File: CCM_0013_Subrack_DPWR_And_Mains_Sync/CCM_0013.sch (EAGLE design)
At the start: 12 parts, among them X15 MAB64

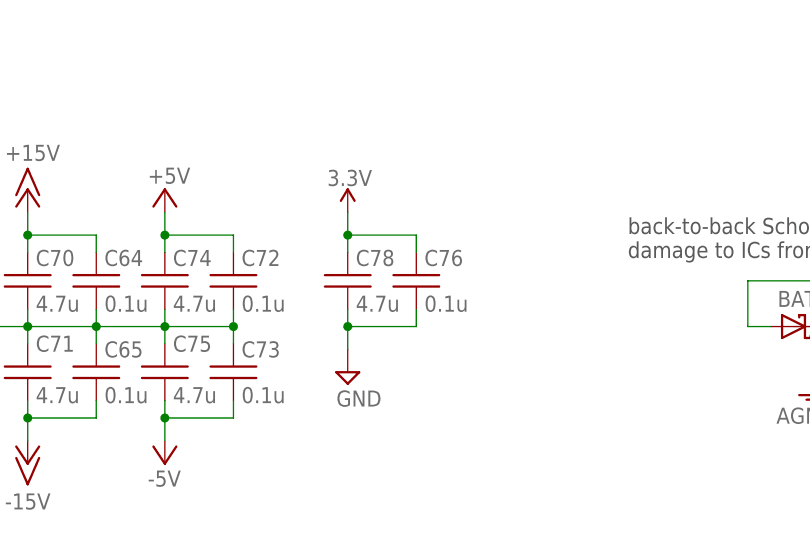
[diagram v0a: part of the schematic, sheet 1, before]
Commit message: Shutter driver added.
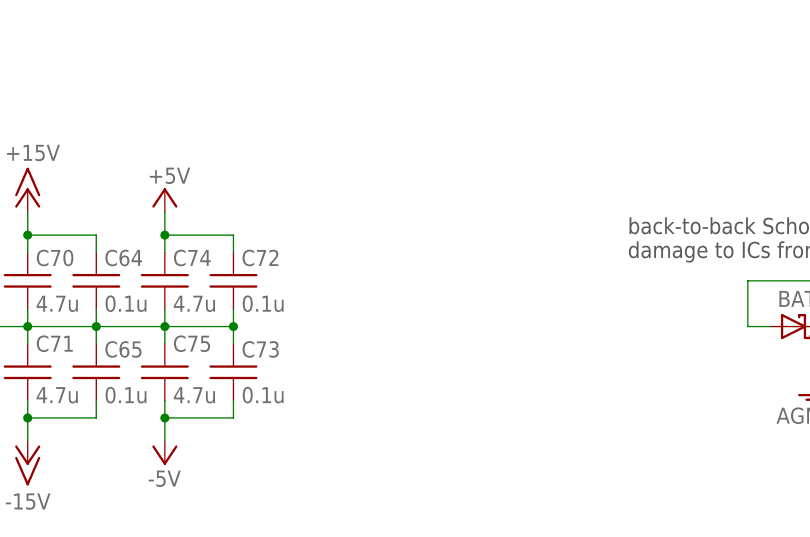
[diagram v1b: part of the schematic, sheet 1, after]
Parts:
- removed C76: 0.1u, acrooptics:C0603
- removed C78: 4.7u, acrooptics:C0603
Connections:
- removed net 3.3V: C76.1, C78.1
- net GND: no longer C76.2, C78.2
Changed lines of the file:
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@@
 <?xml version="1.0" encoding="utf-8"?>
 <!DOCTYPE eagle SYSTEM "eagle.dtd">
-<eagle version="8.6.0">
+<eagle version="9.0.1">
 <drawing>
 <settings>
@@
 <setting verticaltext="up"/>
 </settings>
-<grid distance="0.025" unitdist="inch" unit="inch" style="lines" multiple="4" display="yes" altdistance="0.01" altunitdist="inch" altunit="inch"/>
+<grid distance="0.1" unitdist="inch" unit="inch" style="lines" multiple="1" display="no" altdistance="0.01" altunitdist="inch" altunit="inch"/>
 <layers>
 <layer number="1" name="Top" color="4" fill="1" visible="no" active="no"/>
@@
 <part name="P-28" library="supply1" library_urn="urn:adsk.eagle:library:371" deviceset="-5V" device=""/>
 <part name="P+56" library="acrooptics" deviceset="+5V" device=""/>
-<part name="C76" library="acrooptics" deviceset="C" device="0603" value="0.1u"/>
-<part name="C78" library="acrooptics" deviceset="C" device="0603" value="4.7u"/>
-<part name="P+61" library="SparkFun" deviceset="3.3V" device=""/>
-<part name="SUPPLY29" library="acrooptics" deviceset="GND" device=""/>
 <part name="D9" library="diode" library_urn="urn:adsk.eagle:library:210" deviceset="BAT54S" device="" package3d_urn="urn:adsk.eagle:package:43389/2"/>
 <part name="AGND17" library="supply1" library_urn="urn:adsk.eagle:library:371" deviceset="AGND" device=""/>
@@
 <attribute name="VALUE" x="38.735" y="43.815" size="1.778" layer="96"/>
 </instance>
-<instance part="C76" gate="G$1" x="68.58" y="33.655" smashed="yes">
-<attribute name="NAME" x="69.469" y="34.671" size="1.778" layer="95"/>
-<attribute name="VALUE" x="69.469" y="29.591" size="1.778" layer="96"/>
-</instance>
-<instance part="C78" gate="G$1" x="60.96" y="33.655" smashed="yes">
-<attribute name="NAME" x="61.849" y="34.671" size="1.778" layer="95"/>
-<attribute name="VALUE" x="61.849" y="29.591" size="1.778" layer="96"/>
-</instance>
-<instance part="P+61" gate="G$1" x="60.96" y="40.64" smashed="yes">
-<attribute name="VALUE" x="58.674" y="43.561" size="1.778" layer="96"/>
-</instance>
-<instance part="SUPPLY29" gate="GND" x="60.96" y="22.86" smashed="yes">
-<attribute name="VALUE" x="59.69" y="19.05" size="1.778" layer="96"/>
-</instance>
 <instance part="D9" gate="G$1" x="113.03" y="27.94" rot="MR180"/>
 <instance part="AGND17" gate="VR1" x="113.03" y="20.32" smashed="yes">
@@
 </segment>
 </net>
-<net name="3.3V" class="0">
-<segment>
-<pinref part="C78" gate="G$1" pin="1"/>
-<wire x1="60.96" y1="36.195" x2="60.96" y2="38.1" width="0.1524" layer="91"/>
-<pinref part="C76" gate="G$1" pin="1"/>
-<wire x1="60.96" y1="38.1" x2="68.58" y2="38.1" width="0.1524" layer="91"/>
-<wire x1="68.58" y1="38.1" x2="68.58" y2="36.195" width="0.1524" layer="91"/>
-<pinref part="P+61" gate="G$1" pin="3.3V"/>
-<wire x1="60.96" y1="38.1" x2="60.96" y2="40.64" width="0.1524" layer="91"/>
-<junction x="60.96" y="38.1"/>
-</segment>
-</net>
 <net name="AN0" class="0">
 <segment>
@@
 <net name="GND" class="0">
 <segment>
-<pinref part="C76" gate="G$1" pin="2"/>
-<wire x1="68.58" y1="27.94" x2="68.58" y2="29.845" width="0.1524" layer="91"/>
-<wire x1="68.58" y1="27.94" x2="60.96" y2="27.94" width="0.1524" layer="91"/>
-<pinref part="C78" gate="G$1" pin="2"/>
-<wire x1="60.96" y1="27.94" x2="60.96" y2="29.845" width="0.1524" layer="91"/>
-<pinref part="SUPPLY29" gate="GND" pin="GND"/>
-<wire x1="60.96" y1="27.94" x2="60.96" y2="25.4" width="0.1524" layer="91"/>
-<junction x="60.96" y="27.94"/>
-</segment>
-<segment>
 <pinref part="D9" gate="G$1" pin="A1"/>
